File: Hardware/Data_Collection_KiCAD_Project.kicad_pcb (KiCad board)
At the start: 4 copper layers, 80 x 93.3 mm, 74 parts, among them J1 L717SDC37P1ACH4F, J2 Conn_Coaxial, J3 10118192-0001LF, Q1 SI1040X-T1-GE3, SW1 MCU Reset, U1 BNO055, U2 W25Q32JVSS, U3 MAX-8Q, U4 LP38692MPX-ADJ, U5 USBLC6-2SC6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

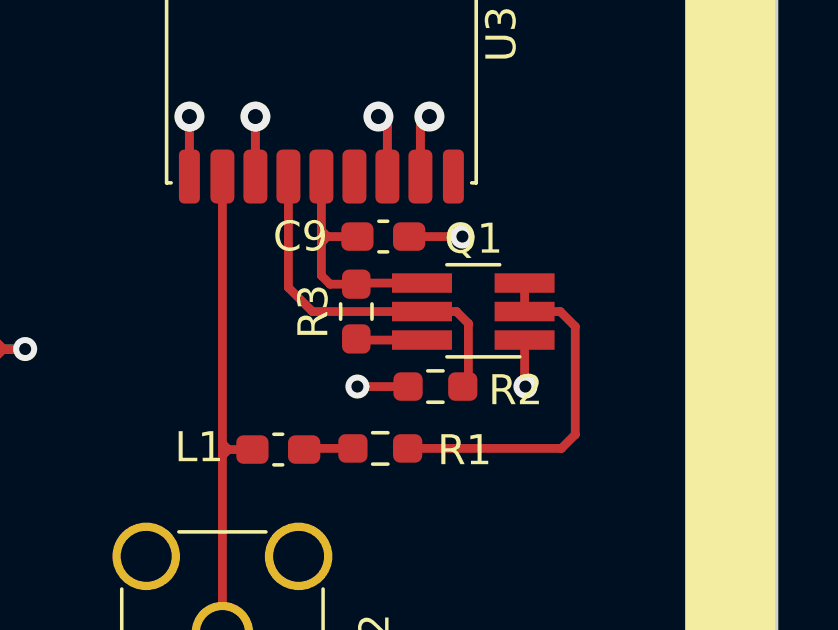
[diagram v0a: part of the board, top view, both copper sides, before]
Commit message: Corrected Si-1040X Footprint
Canged from TSOT-23-6 to SOT-563 (Called SC-89-6 in datasheet)
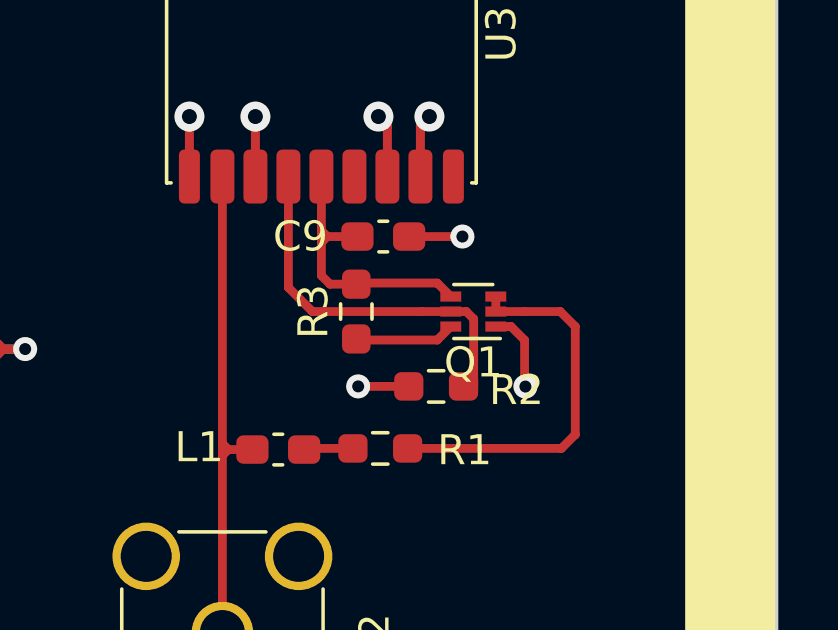
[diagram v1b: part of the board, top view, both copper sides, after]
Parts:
- Q1: footprint Package_TO_SOT_SMD:TSOT-23-6_HandSoldering -> Package_TO_SOT_SMD:SOT-563
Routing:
- net GND: track 136.7 -> 137.8 mm
- net /MAX-8Q/GPS_VCC_RF: track 8.35 -> 9.50 mm
- net Net-(Q1-Pad6): track 2.26 -> 3.35 mm
- net Net-(Q1-Pad2): track 12.4 -> 12.9 mm

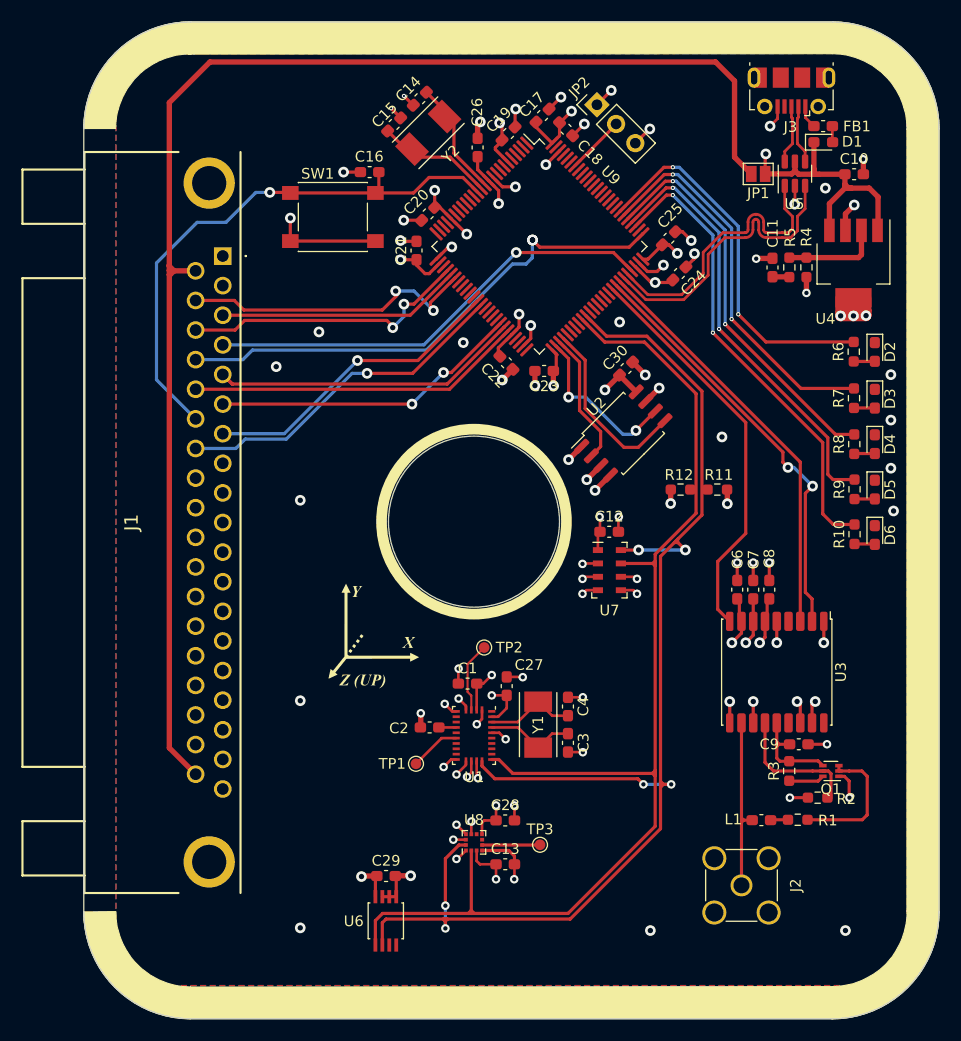
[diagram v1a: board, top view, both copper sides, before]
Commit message: Improved data line separation, added ground stitching vias
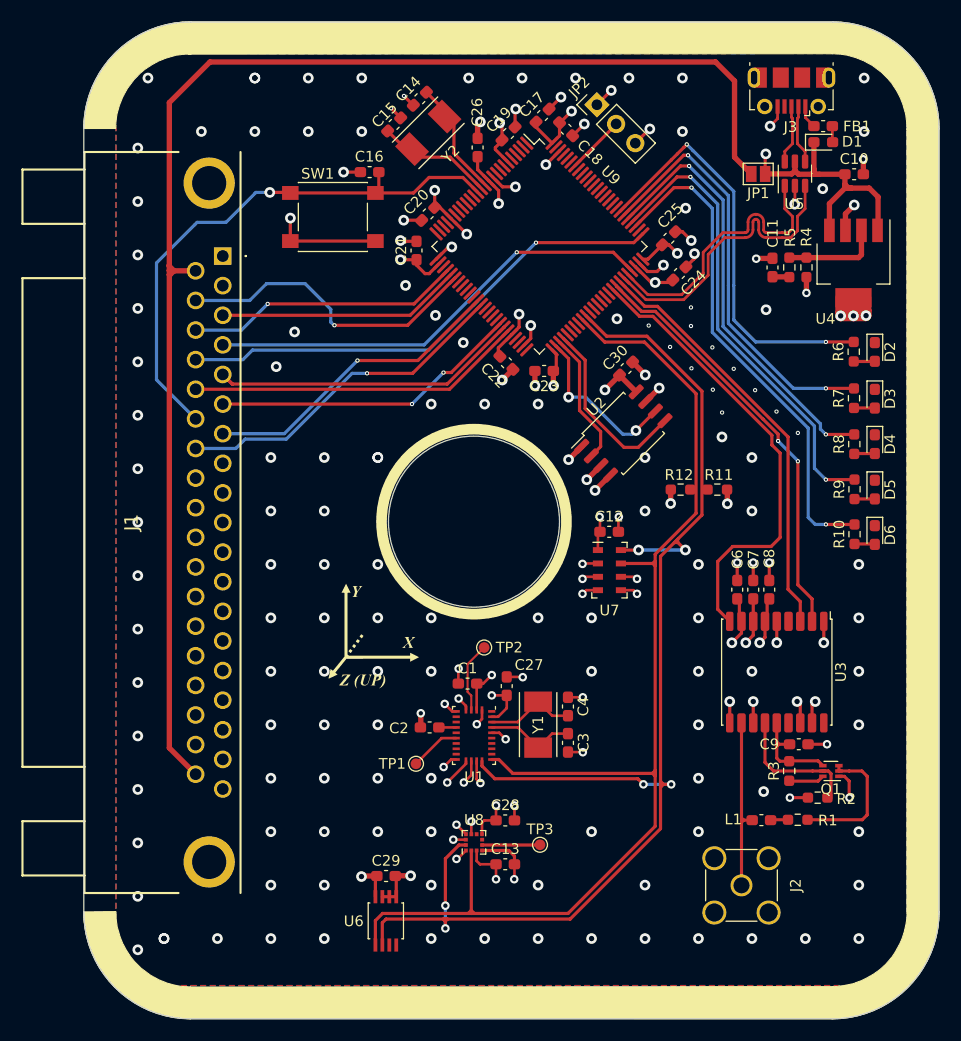
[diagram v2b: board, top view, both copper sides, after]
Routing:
- net /~{GPS_RESET}: track 37.8 -> 43.3 mm
- net Net-(R6-Pad2): track 35.1 -> 39.2 mm
- net Net-(R7-Pad2): track 36.4 -> 39.9 mm
- net Net-(R8-Pad2): track 37.6 -> 40.9 mm
- net Net-(R10-Pad2): track 43.8 -> 46.7 mm
- net Net-(R9-Pad2): track 40.8 -> 43.5 mm
- net GND: track 137.8 -> 140.1 mm, vias 84 -> 196
- net /SWCLK: track 48.6 -> 46.7 mm, vias 2 -> 1
- net /TELEMETRY_SCK: track 27.2 -> 25.9 mm, vias 2 -> 1
- net /GPS_RX: track 38.7 -> 39.4 mm
- net /TELEMETRY_MOSI: vias 2 -> 1

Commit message: Added silkscreen art, adjusted copper pour clearances
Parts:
- added G***: LOGO, RDT_Graphics:RDT_Logo, B.Cu at (102.7, 98.5)
- moved G*** 2.47 mm to (107.7, 111.4)
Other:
- board text added: "3V3"
- board text added: "5V"
- board text added: "Disconnect"
- board text added: "GND"
- board text added: "GPS Antenna"
- board text added: "RESET"

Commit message: Added more silkscreen art
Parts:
- removed the G*** at (107.7, 111.4)
- added G***: LOGO, RDT_Graphics:RDT_Rocket, F.Cu at (102.0, 86.5)
- added G***: LOGO, RDT_Graphics:MEMS_Orientation, F.Cu at (105.5, 111.5)
- added G***: LOGO, RDT_Graphics:GPS, F.Cu at (151.0, 132.5)
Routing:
- net GND: vias 196 -> 197
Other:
- board text added: "Accelerometers"
- board text added: "Barometer"
- board text added: "Bootloader"
- board text added: "Flash Storage"
- board text added: "GPS Module"
- board text added: "High-G"
- board text added: "Low-G"
- board text added: "Temperature"

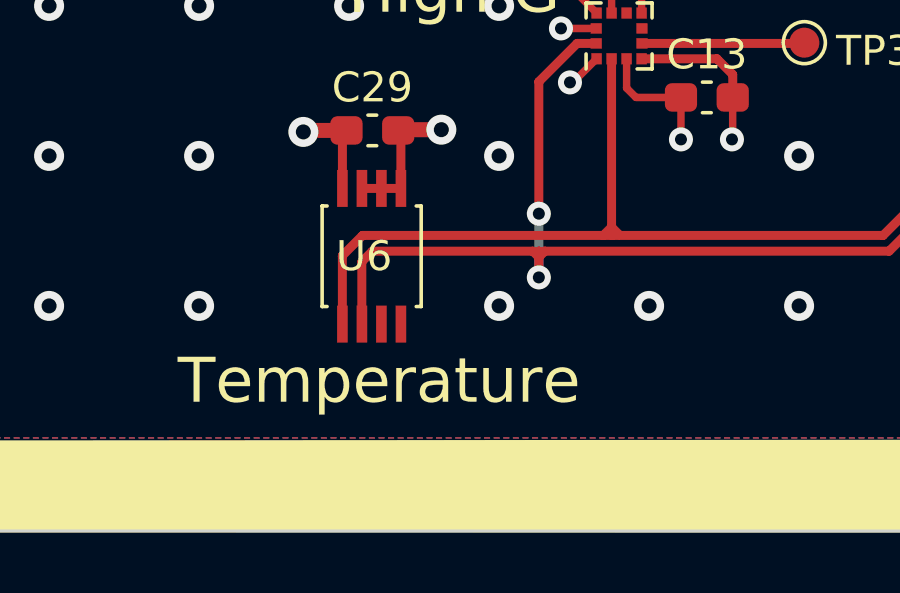
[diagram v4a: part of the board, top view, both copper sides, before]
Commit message: fixed broken layer fill
pad was unconnected due to DRC violation due to copper pour keep out zone.
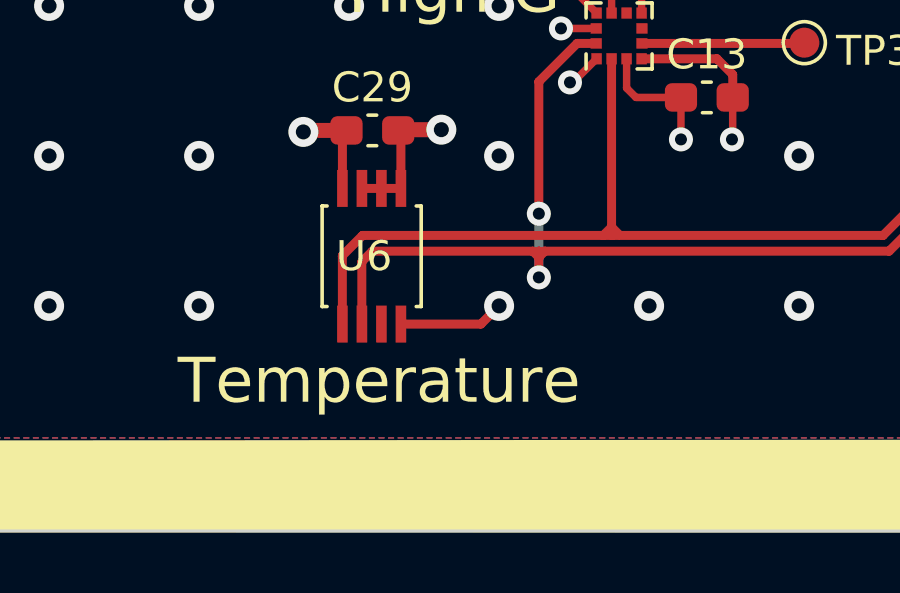
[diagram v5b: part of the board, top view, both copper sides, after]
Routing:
- net GND: track 140.1 -> 143.7 mm
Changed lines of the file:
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@@
   (segment (start 128.095 103.66) (end 126.84 103.66) (width 0.25) (layer "F.Cu") (net 103))
   (segment (start 111.525 116.425) (end 111.525 117.7125) (width 0.5) (layer "F.Cu") (net 103))
+  (segment (start 111.895 138.105) (end 112.5 137.5) (width 0.3) (layer "F.Cu") (net 103))
   (segment (start 128.378428 93.244597) (end 128.378428 93.246572) (width 0.5) (layer "F.Cu") (net 103))
   (segment (start 113.925001 73) (end 114.125001 72.8) (width 0.3) (layer "F.Cu") (net 103))
@@
   (segment (start 129.257377 94.142623) (end 127.825 95.575) (width 0.5) (layer "F.Cu") (net 103))
   (segment (start 142.625 117.325001) (end 142.624999 115.324999) (width 0.3) (layer "F.Cu") (net 103))
+  (segment (start 109.227499 138.105) (end 111.895 138.105) (width 0.3) (layer "F.Cu") (net 103))
   (segment (start 115.7375 128.250001) (end 114.5625 128.250001) (width 0.25) (layer "F.Cu") (net 103))
   (via (at 152.5 112.499999) (size 1) (drill 0.5) (layers "F.Cu" "B.Cu") (free) (net 103))
